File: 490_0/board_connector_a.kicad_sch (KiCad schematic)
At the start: 28 parts, among them J23 DF40C-100DS-0.4V_51_, J4 DF40C-100DS-0.4V_51_, Q6 NMOS, SW8 SW_DPST_x2

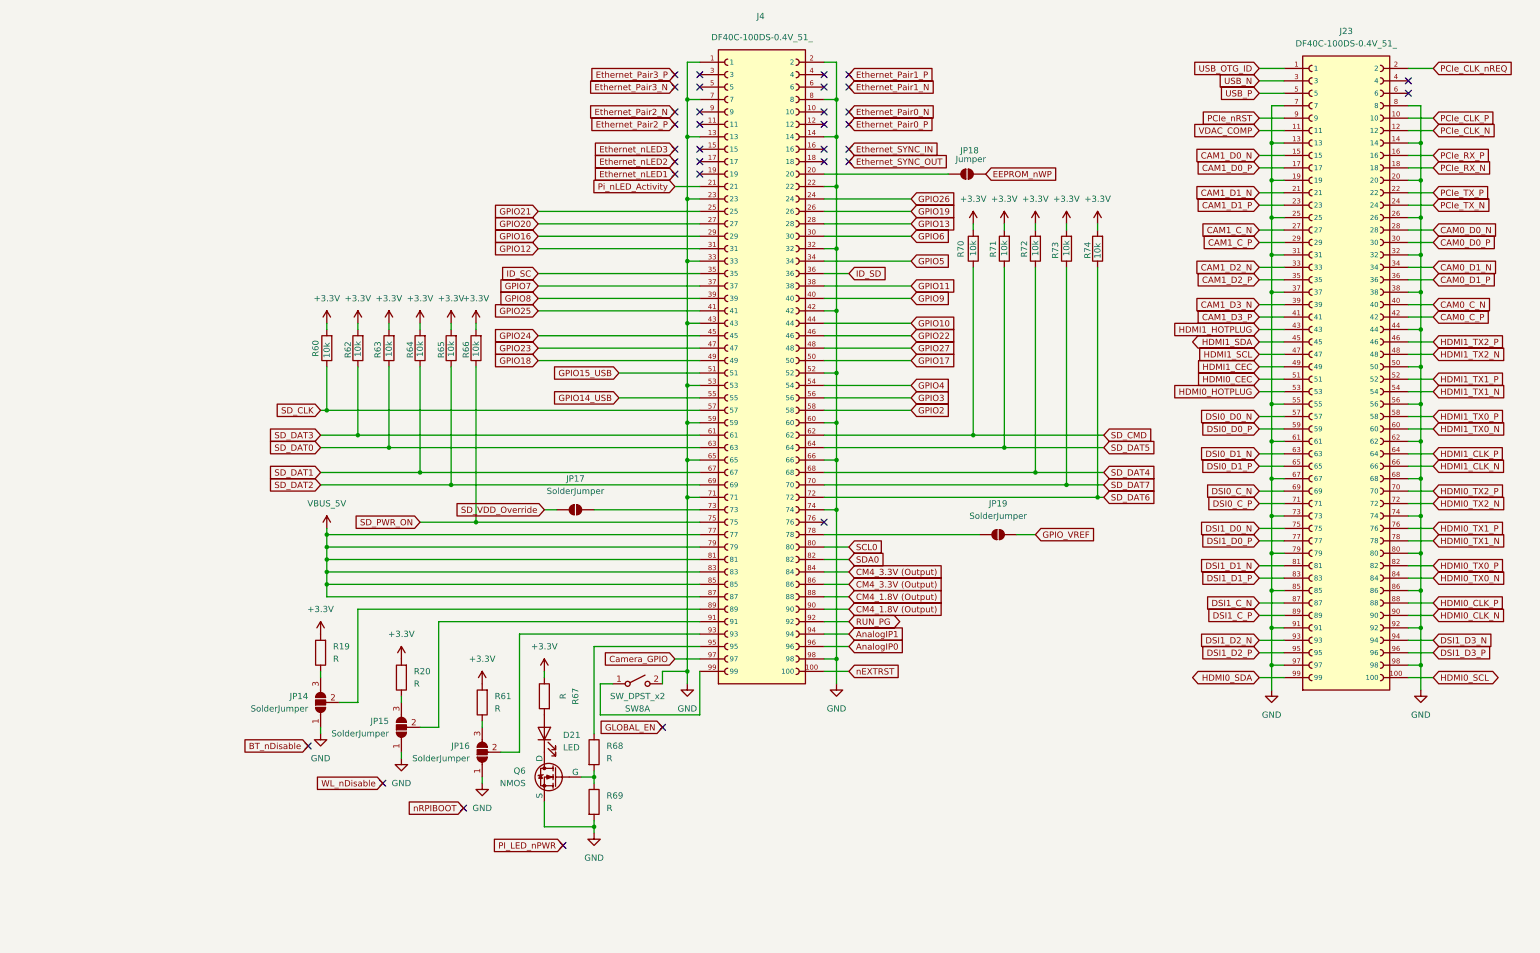
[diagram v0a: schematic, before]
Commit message: US letter format
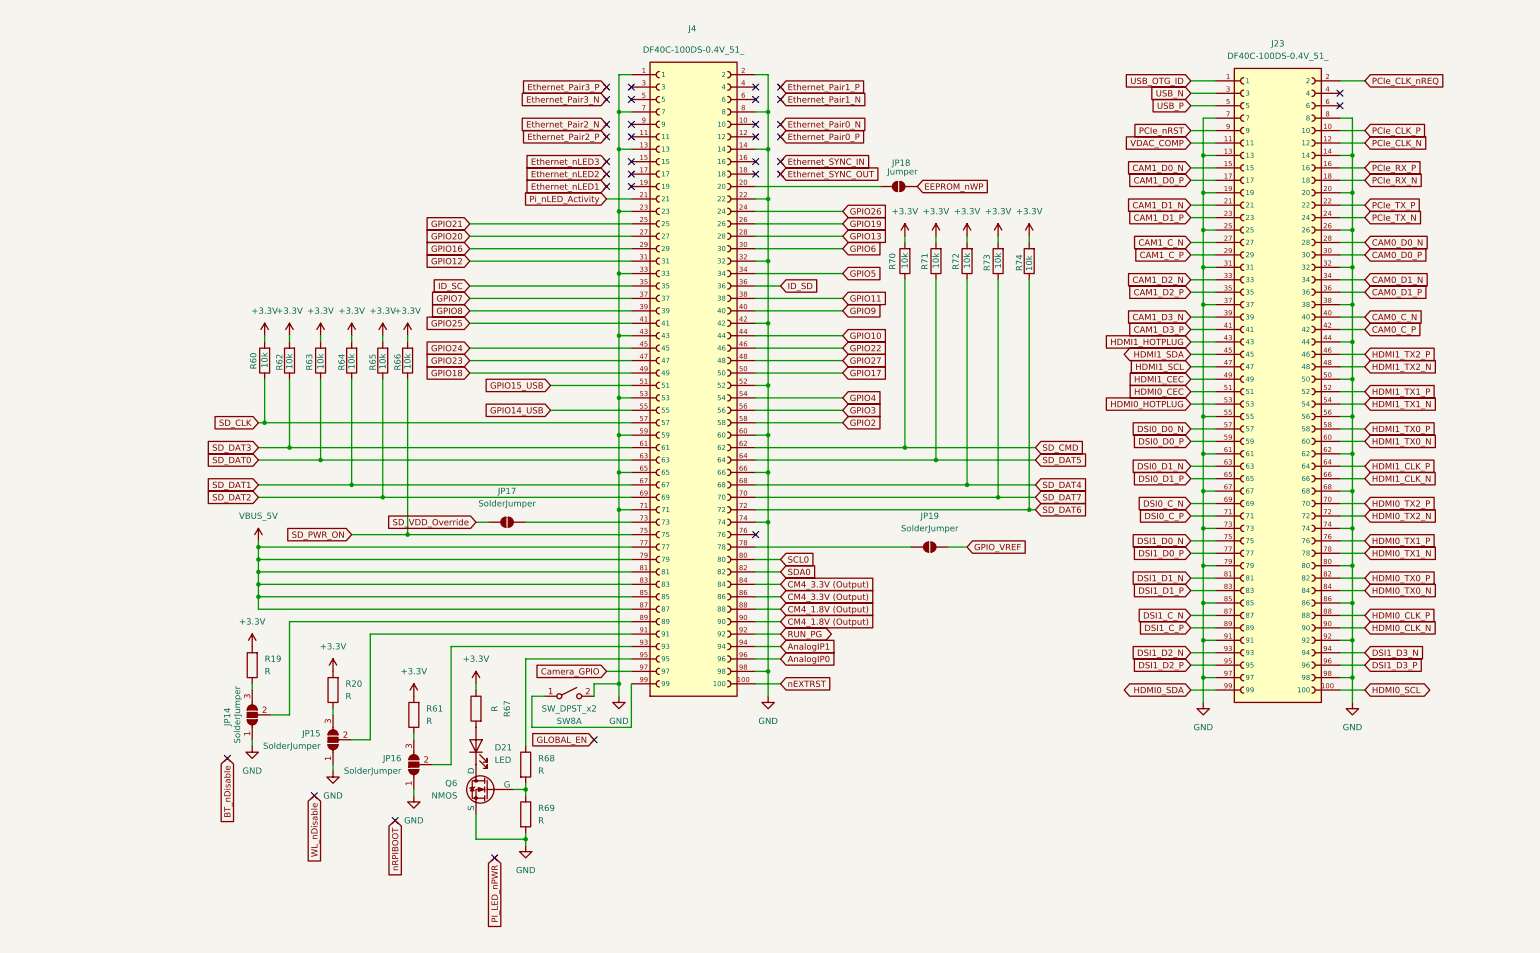
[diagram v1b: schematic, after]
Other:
- moved on the sheet: D21, J23, J4, JP14, JP15, JP16, JP17, JP18, JP19, Q6, R19, R20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

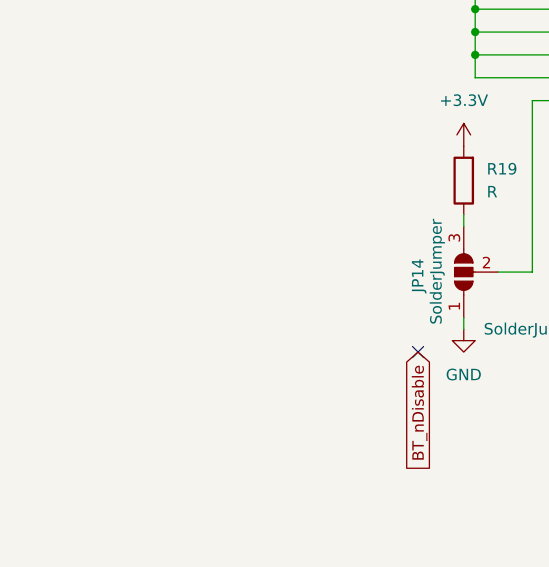
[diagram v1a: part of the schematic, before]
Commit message: Changed some local labels to the right format
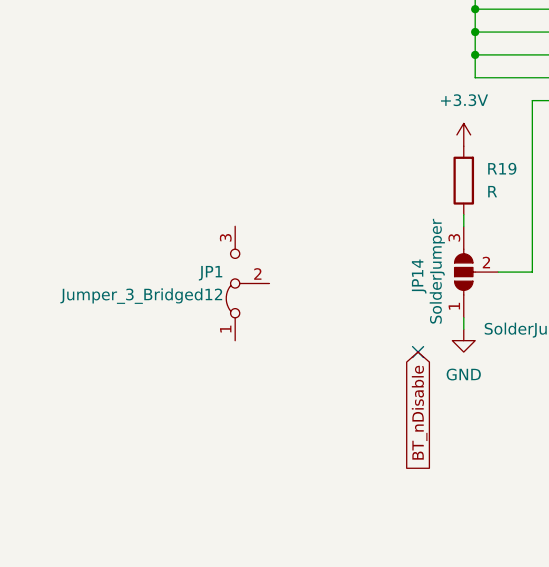
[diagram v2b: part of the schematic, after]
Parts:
- added JP1: Jumper_3_Bridged12, symbol Jumper:Jumper_3_Bridged12
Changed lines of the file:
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@@
+	)
+	(symbol
+		(lib_id "Jumper:Jumper_3_Bridged12")
+		(at -3.81 158.75 90)
+		(unit 1)
+		(exclude_from_sim no)
+		(in_bom no)
+		(on_board yes)
+		(dnp no)
+		(fields_autoplaced yes)
+		(property "Reference" "JP1"
+			(at -5.08 157.4799 90)
+			(effects
+				(font
+					(size 1.27 1.27)
+				)
+				(justify left)
+			)
+		)
+		(property "Value" "Jumper_3_Bridged12"
+			(at -5.08 160.0199 90)
+			(effects
+				(font
+					(size 1.27 1.27)
+				)
+				(justify left)
+			)
+		)
+		(property "Footprint" ""
+			(at -3.81 158.75 0)
+			(effects
+				(font
+					(size 1.27 1.27)
+				)
+				(hide yes)
+			)
+		)
+		(property "Datasheet" "~"
+			(at -3.81 158.75 0)
+			(effects
+				(font
+					(size 1.27 1.27)
+				)
+				(hide yes)
+			)
+		)
+		(property "Description" "Jumper, 3-pole, pins 1+2 closed/bridged"
+			(at -3.81 158.75 0)
+			(effects
+				(font
+					(size 1.27 1.27)
+				)
+				(hide yes)
+			)
+		)
+		(pin "1"
+		)
+		(pin "3"
+		)
+		(pin "2"
+		)
+		(instances
+			(project ""
+				(path "/365a82ed-827d-43e1-aa2f-b98221c4179c/57a94eab-3ef7-4459-81a7-ccf0f968a3f9"
+					(reference "JP1")
+					(unit 1)
+				)
+			)
+		)
 	)
 	(symbol

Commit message: Update board_connector_a.kicad_sch
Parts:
- removed JP1: Jumper_3_Bridged12, symbol Jumper:Jumper_3_Bridged12
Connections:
- net at Q6.2 (G), R68.2: no longer R69.1
- net at J4.95, R68.1: now also R69.1
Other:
- moved on the sheet: R69
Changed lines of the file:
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@@
 	)
 	(junction
-		(at 215.9 43.18)
+		(at 77.47 162.56)
 		(diameter 0)
 		(color 0 0 0 0)
 	)
 	(junction
-		(at 77.47 172.72)
+		(at 215.9 43.18)
 		(diameter 0)
 		(color 0 0 0 0)
@@
 	)
 	(no_connect
-		(at 91.44 162.56)
+		(at 102.87 163.83)
 	)
 	(no_connect
@@
 	(wire
 		(pts
+			(xy 87.63 175.26) (xy 87.63 162.56)
+		)
+		(stroke
+			(width 0)
+			(type default)
+		)
+	)
+	(wire
+		(pts
 			(xy 29.21 88.9) (xy 29.21 102.87)
 		)
@@
 	(wire
 		(pts
-			(xy 77.47 181.61) (xy 77.47 182.88)
-		)
-		(stroke
-			(width 0)
-			(type default)
-		)
-	)
-	(wire
-		(pts
 			(xy 248.92 132.08) (xy 243.84 132.08)
 		)
@@
 	(wire
 		(pts
+			(xy 77.47 182.88) (xy 87.63 182.88)
+		)
+		(stroke
+			(width 0)
+			(type default)
+		)
+	)
+	(wire
+		(pts
 			(xy 66.04 57.15) (xy 99.06 57.15)
 		)
@@
 	(wire
 		(pts
+			(xy 87.63 162.56) (xy 77.47 162.56)
+		)
+		(stroke
+			(width 0)
+			(type default)
+		)
+	)
+	(wire
+		(pts
 			(xy 243.84 43.18) (xy 246.38 43.18)
 		)
@@
 	(wire
 		(pts
+			(xy 77.47 162.56) (xy 77.47 163.83)
+		)
+		(stroke
+			(width 0)
+			(type default)
+		)
+	)
+	(wire
+		(pts
 			(xy 53.34 88.9) (xy 53.34 120.65)
 		)
@@
 	(wire
 		(pts
-			(xy 77.47 146.05) (xy 77.47 163.83)
+			(xy 77.47 146.05) (xy 77.47 162.56)
 		)
 		(stroke
@@
 	(wire
 		(pts
-			(xy 77.47 172.72) (xy 77.47 173.99)
-		)
-		(stroke
-			(width 0)
-			(type default)
-		)
-	)
-	(wire
-		(pts
 			(xy 215.9 50.8) (xy 215.9 58.42)
 		)
@@
 	(global_label "GLOBAL_EN"
 		(shape input)
-		(at 91.44 162.56 180)
+		(at 102.87 163.83 180)
 		(effects
 			(font
@@
 		)
 		(property "Intersheetrefs" "${INTERSHEET_REFS}"
-			(at 91.44 162.56 0)
+			(at 102.87 163.83 0)
 			(effects
 				(font
@@
 	)
 	(symbol
-		(lib_id "Jumper:Jumper_3_Bridged12")
-		(at -3.81 158.75 90)
-		(unit 1)
-		(exclude_from_sim no)
-		(in_bom no)
-		(on_board yes)
-		(dnp no)
-		(fields_autoplaced yes)
-		(property "Reference" "JP1"
-			(at -5.08 157.4799 90)
-			(effects
-				(font
-					(size 1.27 1.27)
-				)
-				(justify left)
-			)
-		)
-		(property "Value" "Jumper_3_Bridged12"
-			(at -5.08 160.0199 90)
-			(effects
-				(font
-					(size 1.27 1.27)
-				)
-				(justify left)
-			)
-		)
-		(property "Footprint" ""
-			(at -3.81 158.75 0)
-			(effects
-				(font
-					(size 1.27 1.27)
-				)
-				(hide yes)
-			)
-		)
-		(property "Datasheet" "~"
-			(at -3.81 158.75 0)
-			(effects
-				(font
-					(size 1.27 1.27)
-				)
-				(hide yes)
-			)
-		)
-		(property "Description" "Jumper, 3-pole, pins 1+2 closed/bridged"
-			(at -3.81 158.75 0)
-			(effects
-				(font
-					(size 1.27 1.27)
-				)
-				(hide yes)
-			)
-		)
-		(pin "1"
-		)
-		(pin "3"
-		)
-		(pin "2"
-		)
-		(instances
-			(project ""
-				(path "/365a82ed-827d-43e1-aa2f-b98221c4179c/57a94eab-3ef7-4459-81a7-ccf0f968a3f9"
-					(reference "JP1")
-					(unit 1)
-				)
-			)
-		)
-	)
-	(symbol
 		(lib_id "power:GND")
 		(at 246.38 154.94 0)
@@
 	(symbol
 		(lib_id "Device:R")
-		(at 77.47 177.8 0)
+		(at 87.63 179.07 0)
 		(unit 1)
 		(exclude_from_sim no)
@@
 		(fields_autoplaced yes)
 		(property "Reference" "R69"
-			(at 80.01 176.5299 0)
+			(at 90.17 177.7999 0)
 			(effects
 				(font
@@
 		)
 		(property "Value" "R"
-			(at 80.01 179.0699 0)
+			(at 90.17 180.3399 0)
 			(effects
 				(font
@@
 		)
 		(property "Footprint" ""
-			(at 75.692 177.8 90)
+			(at 85.852 179.07 90)
 			(effects
 				(font
@@
 		)
 		(property "Datasheet" "~"
-			(at 77.47 177.8 0)
+			(at 87.63 179.07 0)
 			(effects
 				(font
@@
 		)
 		(property "Description" "Resistor"
-			(at 77.47 177.8 0)
+			(at 87.63 179.07 0)
 			(effects
 				(font

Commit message: Minor fixes
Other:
- note added: "BT_nDisable"
- note added: "PI_LED_nPWR"
- note added: "WL_nDisable"
- note added: "nRPIBOOT"
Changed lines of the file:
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@@
 	(generator_version "9.0")
 	(paper "USLetter")
+	(text "nRPIBOOT"
+		(exclude_from_sim no)
+		(at 51.054 185.42 90)
+		(effects
+			(font
+				(size 1.27 1.27)
+			)
+		)
+	)
+	(text "PI_LED_nPWR"
+		(exclude_from_sim no)
+		(at 71.374 194.564 90)
+		(effects
+			(font
+				(size 1.27 1.27)
+			)
+		)
+	)
+	(text "WL_nDisable\n"
+		(exclude_from_sim no)
+		(at 34.036 181.102 90)
+		(effects
+			(font
+				(size 1.27 1.27)
+			)
+		)
+	)
+	(text "BT_nDisable\n"
+		(exclude_from_sim no)
+		(at 16.256 173.736 90)
+		(effects
+			(font
+				(size 1.27 1.27)
+			)
+		)
+	)
 	(junction
 		(at 215.9 104.14)
@@
 		)
 	)
-	(global_label "WL_nDisable"
-		(shape input)
-		(at 34.29 173.99 270)
-		(effects
-			(font
-				(size 1.27 1.27)
-			)
-			(justify right)
-		)
-		(property "Intersheetrefs" "${INTERSHEET_REFS}"
-			(at 34.29 173.99 90)
-			(effects
-				(font
-					(size 1.27 1.27)
-				)
-				(hide yes)
-			)
-		)
-	)
 	(global_label "RUN_PG"
 		(shape bidirectional)
@@
 		)
 	)
-	(global_label "BT_nDisable"
-		(shape input)
-		(at 16.51 166.37 270)
-		(effects
-			(font
-				(size 1.27 1.27)
-			)
-			(justify right)
-		)
-		(property "Intersheetrefs" "${INTERSHEET_REFS}"
-			(at 16.51 166.37 90)
-			(effects
-				(font
-					(size 1.27 1.27)
-				)
-				(justify right)
-				(hide yes)
-			)
-		)
-	)
 	(global_label "DSI1_C_N"
 		(shape input)
@@
 		)
 	)
-	(global_label "nRPIBOOT"
-		(shape input)
-		(at 50.8 179.07 270)
-		(effects
-			(font
-				(size 1.27 1.27)
-			)
-			(justify right)
-		)
-		(property "Intersheetrefs" "${INTERSHEET_REFS}"
-			(at 50.8 179.07 90)
-			(effects
-				(font
-					(size 1.27 1.27)
-				)
-				(hide yes)
-			)
-		)
-	)
 	(global_label "GPIO7"
 		(shape input)
@@
 			(effects
 				(font
-					(size 1.27 1.27)
-				)
-				(hide yes)
-			)
-		)
-	)
-	(global_label "PI_LED_nPWR"
-		(shape input)
-		(at 71.12 186.69 270)
-		(effects
-			(font
-				(size 1.27 1.27)
-			)
-			(justify right)
-		)
-		(property "Intersheetrefs" "${INTERSHEET_REFS}"
-			(at 71.12 186.69 90)
-			(effects
-				(font

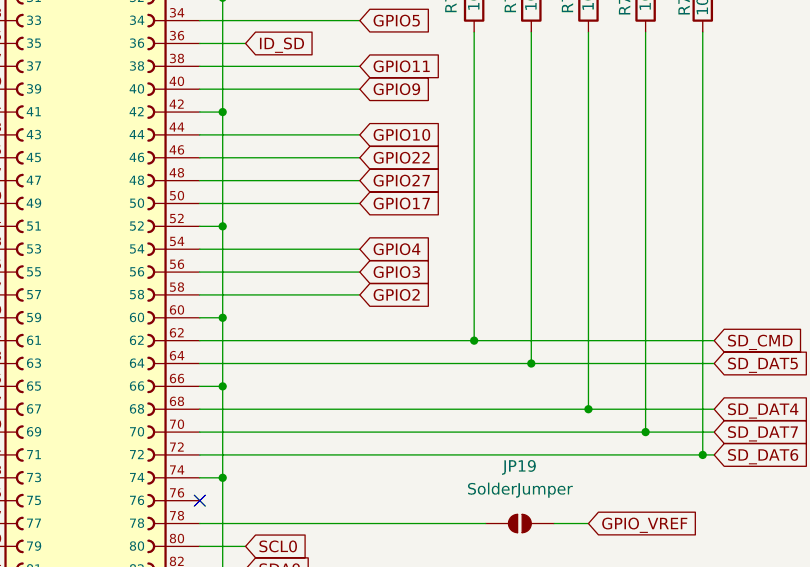
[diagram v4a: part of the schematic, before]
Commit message: Changed the camera connectors
- Added 2 and 4 lane MIPI 22 lane connectors
- Added digikey link to a good type
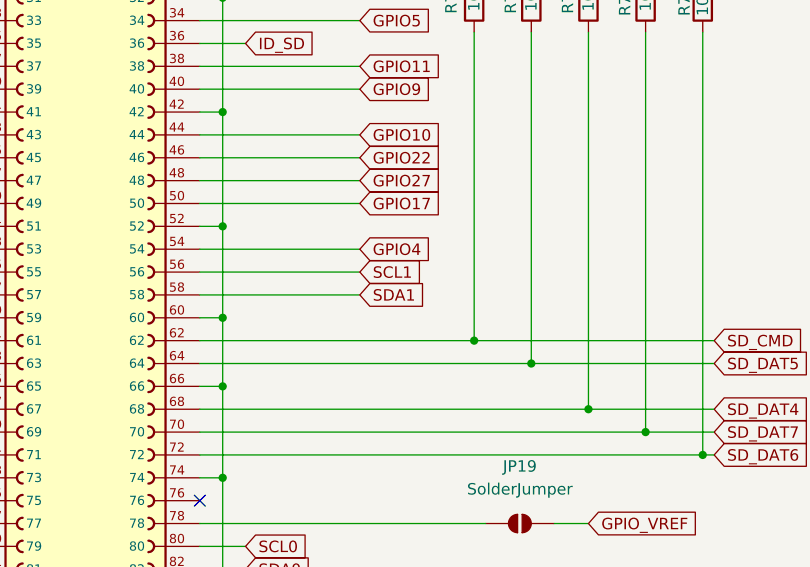
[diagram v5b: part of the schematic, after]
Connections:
- net GPIO2 renamed SDA1
- net GPIO3 renamed SCL1
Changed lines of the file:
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@@
 		)
 	)
-	(global_label "GPIO3"
+	(global_label "SCL1"
 		(shape input)
 		(at 142.24 95.25 0)
@@
 		)
 	)
-	(global_label "GPIO2"
+	(global_label "SDA1"
 		(shape input)
 		(at 142.24 97.79 0)

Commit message: Minor updates
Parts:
- renumbered D21 to D2, J4 to J3, J23 to J4, JP18 to JP1, JP17 to JP2, JP19 to JP3, JP14 to JP4, JP15 to JP5, JP16 to JP6, Q6 to Q2, R72 to R10, R73 to R11, R74 to R12, R60 to R13, R62 to R14, R63 to R15, R64 to R16, R65 to R17, R66 to R18, R67 to R21, R61 to R22, R68 to R23, R69 to R24, R70 to R8, R71 to R9, SW8 to SW1

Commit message: updates
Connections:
- no-connect marks 34 -> 30
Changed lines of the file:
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@@
-	)
-	(no_connect
-		(at 16.51 166.37)
 	)
 	(no_connect
@@
 	)
 	(no_connect
-		(at 34.29 173.99)
-	)
-	(no_connect
 		(at 99.06 46.99)
 	)
@@
 	)
 	(no_connect
-		(at 50.8 179.07)
-	)
-	(no_connect
 		(at 129.54 44.45)
 	)
 	(no_connect
-		(at 71.12 186.69)
-	)
-	(no_connect
